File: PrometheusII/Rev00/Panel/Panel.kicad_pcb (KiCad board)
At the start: 2 copper layers, 40.3 x 128.5 mm, 0 parts

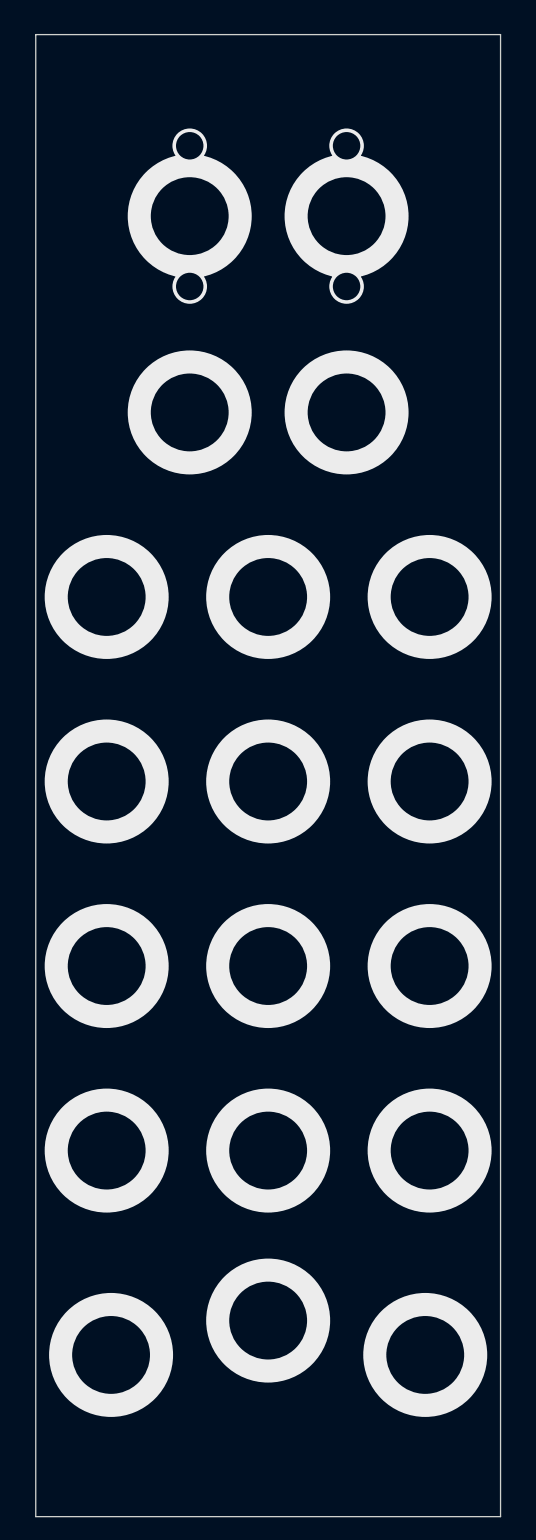
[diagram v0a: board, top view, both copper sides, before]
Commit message: Added mounting holes
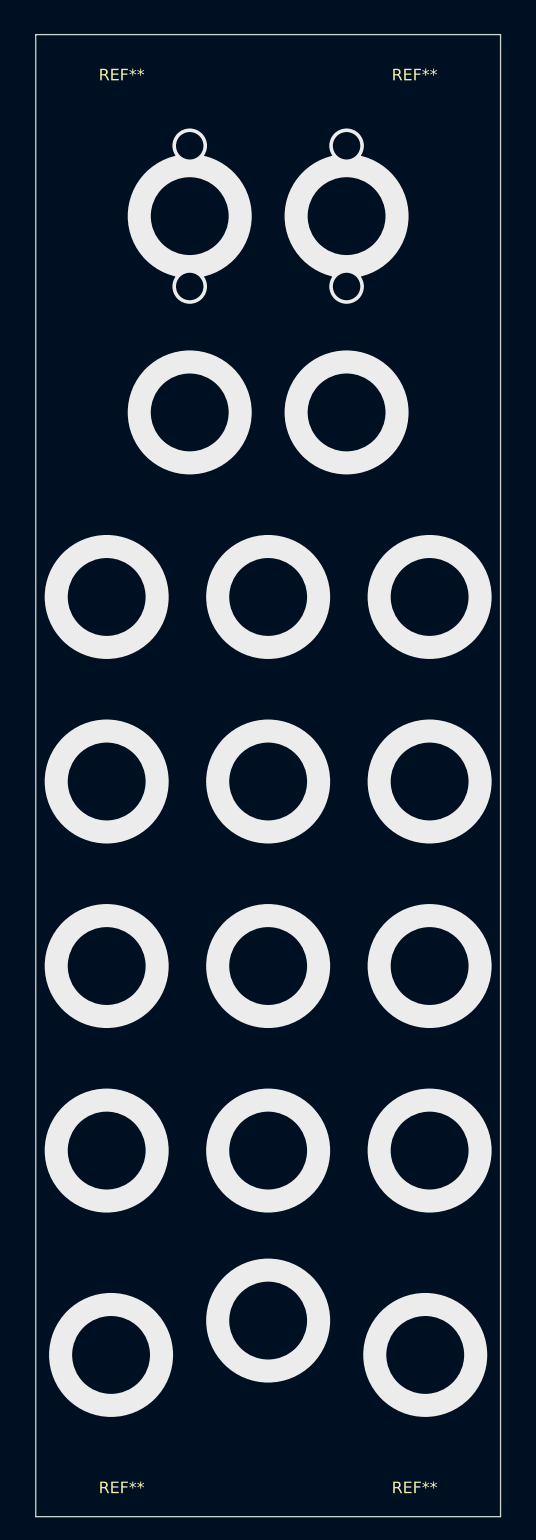
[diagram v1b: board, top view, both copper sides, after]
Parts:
- added REF**: euro_mounting_hole, ttt_lib:euro_mounting_hole, F.Cu at (112.7, 24.5)
- added REF**: euro_mounting_hole, ttt_lib:euro_mounting_hole, F.Cu at (87.3, 24.5)
- added REF**: euro_mounting_hole, ttt_lib:euro_mounting_hole, F.Cu at (87.3, 147.0)
- added REF**: euro_mounting_hole, ttt_lib:euro_mounting_hole, F.Cu at (112.7, 147.0)
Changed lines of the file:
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@@
     (tracks 23)
     (zones 0)
-    (modules 0)
+    (modules 4)
     (nets 1)
   )
@@
     (uvia_drill 0.1)
   )
+  (module ttt_lib:euro_mounting_hole (layer F.Cu)
+    (at 112.7 24.5)
+    (fp_text reference REF** (at 0 0.5) (layer F.SilkS)
+      (effects (font (size 1 1) (thickness 0.15)))
+    )
+    (fp_text value euro_mounting_hole (at 0 -0.5) (layer F.Fab)
+      (effects (font (size 1 1) (thickness 0.15)))
+    )
+    (pad "" np_thru_hole oval (at 0 0) (size 4.8 3.2) (drill oval 4.8 3.2) (layers *.Cu *.Mask))
+  )
+  (module ttt_lib:euro_mounting_hole (layer F.Cu)
+    (at 87.3 24.5)
+    (fp_text reference REF** (at 0 0.5) (layer F.SilkS)
+      (effects (font (size 1 1) (thickness 0.15)))
+    )
+    (fp_text value euro_mounting_hole (at 0 -0.5) (layer F.Fab)
+      (effects (font (size 1 1) (thickness 0.15)))
+    )
+    (pad "" np_thru_hole oval (at 0 0) (size 4.8 3.2) (drill oval 4.8 3.2) (layers *.Cu *.Mask))
+  )
+  (module ttt_lib:euro_mounting_hole (layer F.Cu)
+    (at 87.3 147)
+    (fp_text reference REF** (at 0 0.5) (layer F.SilkS)
+      (effects (font (size 1 1) (thickness 0.15)))
+    )
+    (fp_text value euro_mounting_hole (at 0 -0.5) (layer F.Fab)
+      (effects (font (size 1 1) (thickness 0.15)))
+    )
+    (pad "" np_thru_hole oval (at 0 0) (size 4.8 3.2) (drill oval 4.8 3.2) (layers *.Cu *.Mask))
+  )
+  (module ttt_lib:euro_mounting_hole (layer F.Cu)
+    (at 112.7 147)
+    (fp_text reference REF** (at 0 0.5) (layer F.SilkS)
+      (effects (font (size 1 1) (thickness 0.15)))
+    )
+    (fp_text value euro_mounting_hole (at 0 -0.5) (layer F.Fab)
+      (effects (font (size 1 1) (thickness 0.15)))
+    )
+    (pad "" np_thru_hole oval (at 0 0) (size 4.8 3.2) (drill oval 4.8 3.2) (layers *.Cu *.Mask))
+  )
   (gr_line (start 120.15 21.5) (end 79.85 21.5) (layer Edge.Cuts) (width 0.05))

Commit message: Initial panel design
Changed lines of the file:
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@@
   (general
     (thickness 1.6)
-    (drawings 4)
+    (drawings 22)
     (tracks 23)
     (zones 0)
@@
   (layers
     (0 F.Cu signal)
-    (31 B.Cu signal)
+    (31 B.Cu signal hide)
     (32 B.Adhes user)
     (33 F.Adhes user)
     (34 B.Paste user)
     (35 F.Paste user)
-    (36 B.SilkS user)
+    (36 B.SilkS user hide)
     (37 F.SilkS user)
     (38 B.Mask user)
@@
       (layerselection 0x010fc_ffffffff)
       (usegerberextensions false)
-      (usegerberattributes false)
+      (usegerberattributes true)
       (usegerberadvancedattributes false)
       (creategerberjobfile false)
-      (excludeedgelayer true)
-      (linewidth 0.100000)
+      (excludeedgelayer false)
+      (linewidth 0.150000)
       (plotframeref false)
       (viasonmask false)
       (mode 1)
-      (useauxorigin false)
+      (useauxorigin true)
       (hpglpennumber 1)
       (hpglpenspeed 20)
@@
       (outputformat 1)
       (mirror false)
-      (drillshape 1)
+      (drillshape 0)
       (scaleselection 1)
       (outputdirectory ""))
@@
     (pad "" np_thru_hole oval (at 0 0) (size 4.8 3.2) (drill oval 4.8 3.2) (layers *.Cu *.Mask))
   )
+  (gr_line (start 85 21.5) (end 85 62.25) (layer F.SilkS) (width 2))
+  (gr_line (start 115 62.25) (end 115 21.5) (layer F.SilkS) (width 2))
+  (gr_poly (pts (xy 79.75 125.5) (xy 120.25 125.5) (xy 120.25 150) (xy 79.75 150)) (layer F.Cu) (width 0))
+  (gr_poly (pts (xy 85 21.5) (xy 115 21.5) (xy 115 62.5) (xy 85 62.5)) (layer F.Mask) (width 0))
+  (gr_line (start 79.75 125.5) (end 120.25 125.5) (layer F.SilkS) (width 2))
+  (gr_line (start 107 125.5) (end 107 62.5) (layer F.SilkS) (width 2))
+  (gr_line (start 93 62.25) (end 93 125.5) (layer F.SilkS) (width 2))
+  (gr_line (start 120.25 62.25) (end 79.75 62.25) (layer F.SilkS) (width 2))
+  (gr_poly (pts (xy 79.75 62.25) (xy 120.25 62.25) (xy 120.25 125.5) (xy 80 125.5) (xy 79.75 125.5)) (layer F.Mask) (width 0))
+  (gr_poly (pts (xy 120.25 62.25) (xy 120.25 125.5) (xy 107 125.5) (xy 107 62.25)) (layer F.Cu) (width 0))
+  (gr_poly (pts (xy 93 62.25) (xy 93 125.5) (xy 79.75 125.5) (xy 79.75 62.25)) (layer F.Cu) (width 0))
+  (gr_line (start 100.5 125.5) (end 87 125.5) (layer Dwgs.User) (width 0.15))
+  (gr_line (start 85 62.25) (end 92.25 62.25) (layer Dwgs.User) (width 0.15))
+  (gr_line (start 93 67.5) (end 93 74.5) (layer Dwgs.User) (width 0.15))
+  (gr_line (start 93 70) (end 93 67.5) (layer Dwgs.User) (width 0.15))
+  (gr_poly (pts (xy 85 21.5) (xy 85 62.25) (xy 115 62.25) (xy 115 21.5)) (layer F.Cu) (width 0))
+  (gr_line (start 85 21.5) (end 85 62.25) (layer Dwgs.User) (width 0.15))
+  (gr_line (start 85 21.5) (end 115 21.5) (layer Dwgs.User) (width 0.15))
   (gr_line (start 120.15 21.5) (end 79.85 21.5) (layer Edge.Cuts) (width 0.05))
   (gr_line (start 79.85 150) (end 120.15 150) (layer Edge.Cuts) (width 0.05))
